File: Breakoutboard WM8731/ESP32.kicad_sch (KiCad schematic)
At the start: 23 parts

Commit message: more work on the esp part
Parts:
- added D?: SS54, symbol Device:D_Schottky
- added R? (x2): 5.1k, symbol Device:R
- C? (x5): value (none) -> 100n
- C?: value (none) -> 22u
- C?: value (none) -> 4.7u
- J?: value (none) -> USB_C_Receptacle
- Q? (x2): value (none) -> SS8050-G; footprint (none) -> Package_TO_SOT_THT:TO-92_Inline
- R?: value (none) -> 2.2k
- R?: value (none) -> 22k
- R? (x4): value (none) -> 10k
- R?: value (none) -> 47k
- R? (x2): value (none) -> 0
- SW?: value (none) -> SW_Reset
- SW?: value (none) -> SW_Flash
- U?: value (none) -> CP2102N; footprint (none) -> Package_DFN_QFN:QFN-28-1EP_5x5mm_P0.5mm_EP3.35x3.35mm
- U?: value (none) -> ESP32-WROOM-32E; footprint (none) -> XCVR_ESP32-WROOM-32E_(16MB)
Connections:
- net D+: now also J?.A6 (D+), J?.B6 (D+)
- net D-: now also J?.A7 (D-), J?.B7 (D-)
- net GND: now also J?.A1 (GND), J?.A12 (GND), J?.B1 (GND), J?.B12 (GND), J?.S1 (SHIELD), R?.2, R?.2
- net VBUS: now also J?.A4 (VBUS), J?.A9 (VBUS), J?.B4 (VBUS), J?.B9 (VBUS), D?.2 (A)
- net at J?.A5 (CC1): now also R?.1
- net at J?.B5 (CC2): now also R?.1
- new net +5V: D?.1 (K)
- no-connect marks 13 -> 23
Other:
- moved on the sheet: C?, J?, Q?, R?, SW?, U?

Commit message: renamed untitled -> WM8731 Input Output
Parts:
- D?: value SS54 -> (none)
- R? (x2): value 5.1k -> (none)
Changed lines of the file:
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@@
       (effects (font (size 1.27 1.27)) hide)
     )
-    (property "Value" "GND" (id 1) (at 64.77 129.54 0))
+    (property "Value" "" (id 1) (at 64.77 129.54 0))
     (property "Footprint" "" (id 2) (at 64.77 124.46 0)
       (effects (font (size 1.27 1.27)) hide)
@@
       (effects (font (size 1.27 1.27)) (justify left))
     )
-    (property "Value" "5.1k" (id 1) (at 107.95 73.6599 0)
+    (property "Value" "" (id 1) (at 107.95 73.6599 0)
       (effects (font (size 1.27 1.27)) (justify left))
     )
@@
     (in_bom yes) (on_board yes) (fields_autoplaced)
     (property "Reference" "D?" (id 0) (at 95.5675 52.07 0))
-    (property "Value" "SS54" (id 1) (at 95.5675 54.61 0))
+    (property "Value" "" (id 1) (at 95.5675 54.61 0))
     (property "Footprint" "" (id 2) (at 95.25 58.42 0)
       (effects (font (size 1.27 1.27)) hide)
@@
       (effects (font (size 1.27 1.27)) hide)
     )
-    (property "Value" "GND" (id 1) (at 102.87 83.82 0))
+    (property "Value" "" (id 1) (at 102.87 83.82 0))
     (property "Footprint" "" (id 2) (at 102.87 78.74 0)
       (effects (font (size 1.27 1.27)) hide)
@@
       (effects (font (size 1.27 1.27)) (justify right))
     )
-    (property "Value" "5.1k" (id 1) (at 97.79 73.6599 0)
+    (property "Value" "" (id 1) (at 97.79 73.6599 0)
       (effects (font (size 1.27 1.27)) (justify right))
     )

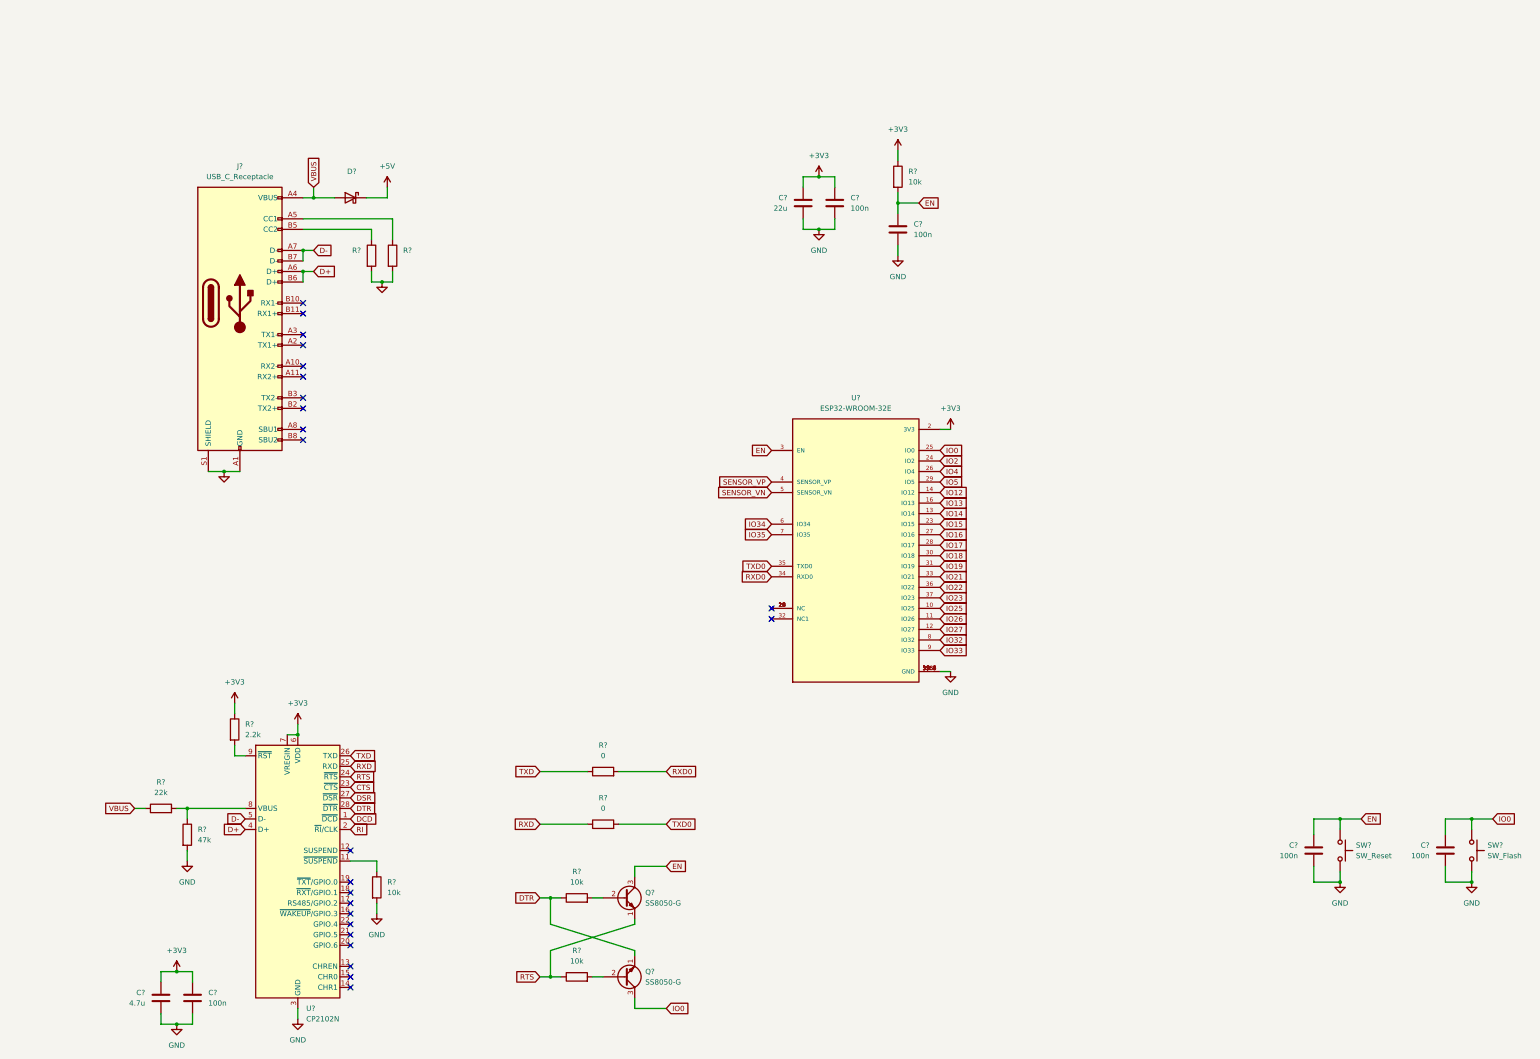
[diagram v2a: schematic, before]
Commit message: reworked power symbols and ESP32 schematic
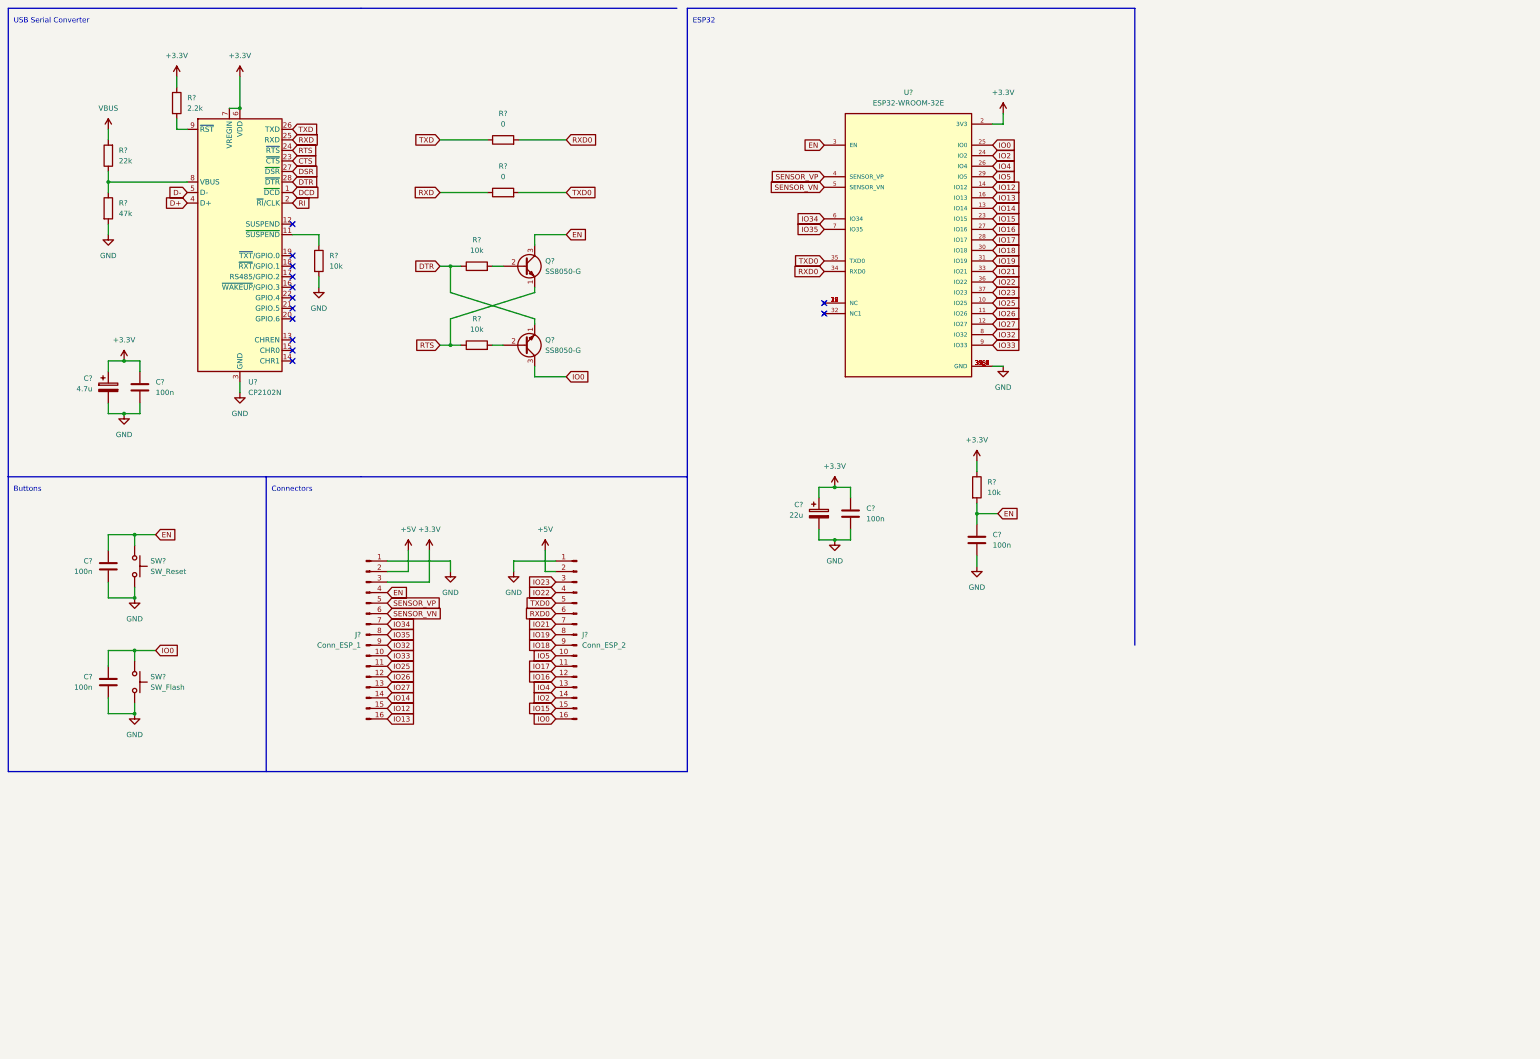
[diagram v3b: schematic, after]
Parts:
- removed C?: 22u, symbol Device:C
- removed C?: 4.7u, symbol Device:C
- removed D?: (no value), symbol Device:D_Schottky
- removed J?: USB_C_Receptacle, symbol Connector:USB_C_Receptacle
- removed R? (x2): (no value), symbol Device:R
- added C?: 4.7u, symbol Device:C_Polarized
- added C?: 22u, symbol Device:C_Polarized
- added J?: Conn_ESP_2, symbol Connector:Conn_01x16_Male
- added J?: Conn_ESP_1, symbol Connector:Conn_01x16_Male
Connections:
- net +3V3: now also C?.1, C?.1, J?.3 (Pin_3)
- net +5V: now also J?.2 (Pin_2), J?.2 (Pin_2)
- net EN: now also J?.4 (Pin_4)
- net GND: now also C?.2, C?.2, J?.1 (Pin_1), J?.1 (Pin_1)
- net IO0: now also J?.16 (Pin_16)
- net IO12: now also J?.15 (Pin_15)
- net IO13: now also J?.16 (Pin_16)
- net IO14: now also J?.14 (Pin_14)
- net IO15: now also J?.15 (Pin_15)
- net IO16: now also J?.12 (Pin_12)
- net IO17: now also J?.11 (Pin_11)
- net IO18: now also J?.9 (Pin_9)
- net IO19: now also J?.8 (Pin_8)
- net IO2: now also J?.14 (Pin_14)
- net IO21: now also J?.7 (Pin_7)
- net IO22: now also J?.4 (Pin_4)
- net IO23: now also J?.3 (Pin_3)
- net IO25: now also J?.11 (Pin_11)
- net IO26: now also J?.12 (Pin_12)
- net IO27: now also J?.13 (Pin_13)
- net IO32: now also J?.9 (Pin_9)
- net IO33: now also J?.10 (Pin_10)
- net IO34: now also J?.7 (Pin_7)
- net IO35: now also J?.8 (Pin_8)
- net IO4: now also J?.13 (Pin_13)
- net IO5: now also J?.10 (Pin_10)
- net RXD0: now also J?.6 (Pin_6)
- net SENSOR_VN: now also J?.6 (Pin_6)
- net SENSOR_VP: now also J?.5 (Pin_5)
- net TXD0: now also J?.5 (Pin_5)
- net VBUS: now also R?.2; no longer R?.1
- net at R?.1, U?.8 (VBUS): now also R?.1; no longer R?.2
- no-connect marks 23 -> 13
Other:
- note added: "Buttons"
- note added: "Connectors"
- note added: "ESP32"
- note added: "USB Serial Converter"
- moved on the sheet: C?, Q?, R?, SW?, U?
